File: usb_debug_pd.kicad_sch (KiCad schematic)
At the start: 83 parts, among them J7 Tag-Connect_TC2050-IDC-NL_2x5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, J8 USB-C_GCT_USB4105-GF-A, Q12 PJE138K, U29 W25Q80DV_USON, U30 TPS65988DHRSHR, U31 NTS0102_XSON, U32 NCP730BMT330_WSON, U34 FT230X_QFN, U39 TPS65988DHRSHR, U40 AP22615A_TSOT26, U42 TPD4E05U06QDQARQ1

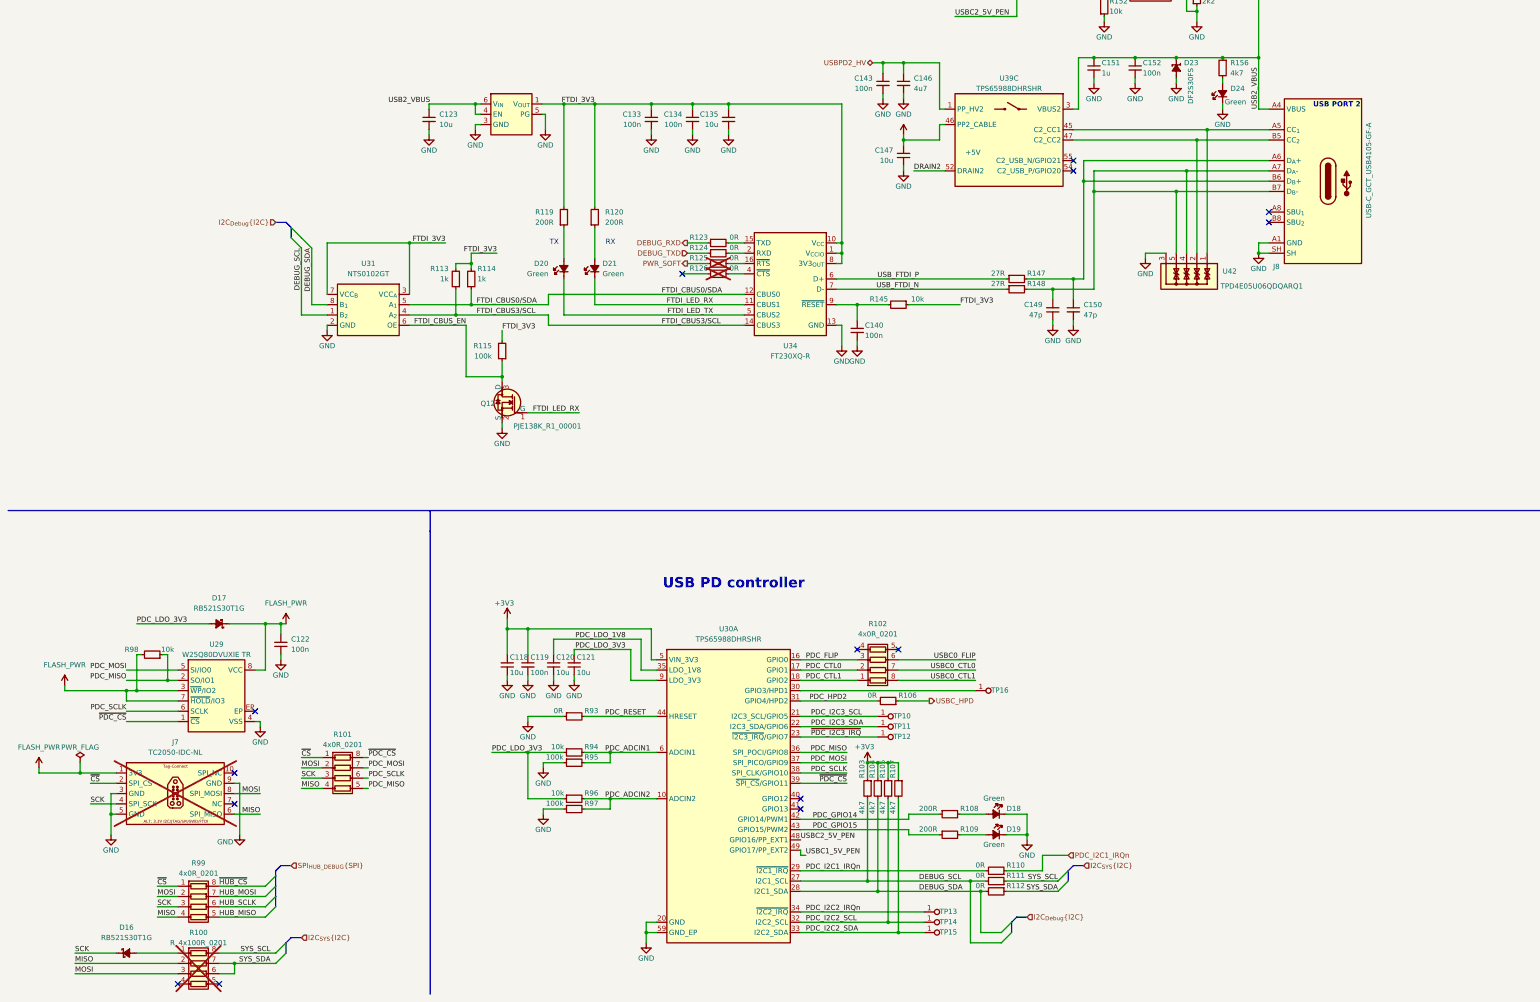
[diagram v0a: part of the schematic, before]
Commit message: [#82837] Start rerouting USB PD controller
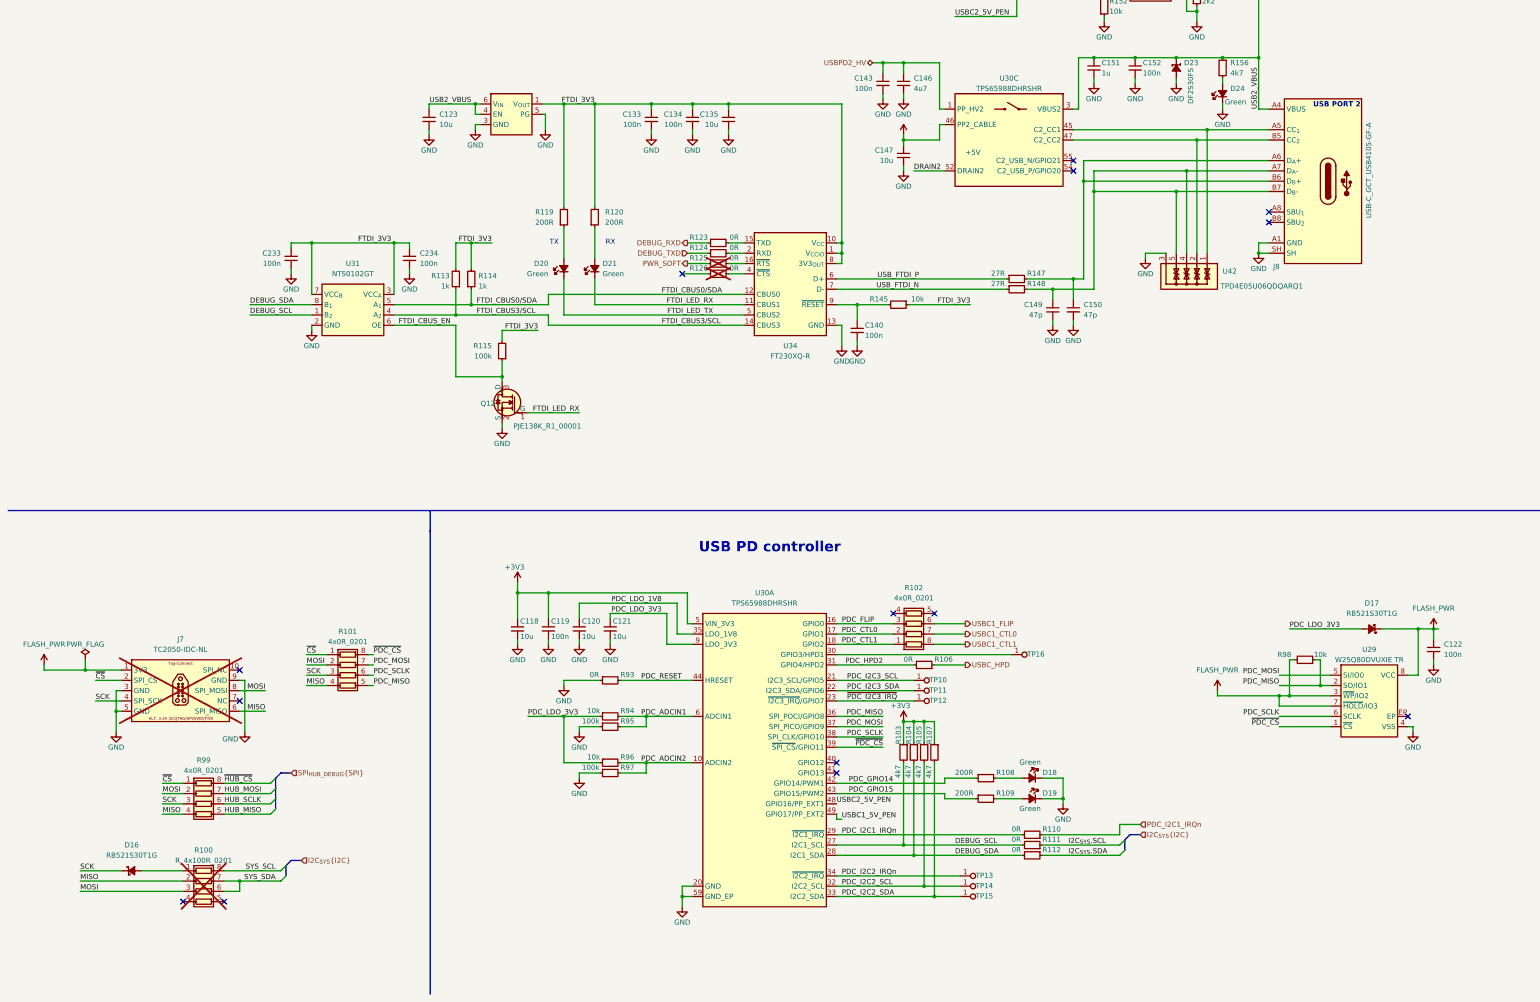
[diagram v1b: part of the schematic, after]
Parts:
- added C233, C234: C_100n_0402, antmicro-footprints:C_0402_1005Metric, symbol antmicroCapacitors0402:C_100n_0402
- renumbered U39 to U30
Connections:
- net FTDI_3V3: now also C233.1, C234.1
- net GND: now also C233.2, C234.2
- net SYS_SCL: no longer R111.1
- net SYS_SDA: no longer R112.1
- net USBC0_CTL0 renamed USBC1_CTL0
- net USBC0_CTL1 renamed USBC1_CTL1
- net USBC0_FLIP renamed USBC1_FLIP
- new net I2C_{SYS}.SCL: R111.1
- new net I2C_{SYS}.SDA: R112.1
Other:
- moved on the sheet: C118, C119, C120, C121, C122, D16, D17, D18, D19, J7, R100, R101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

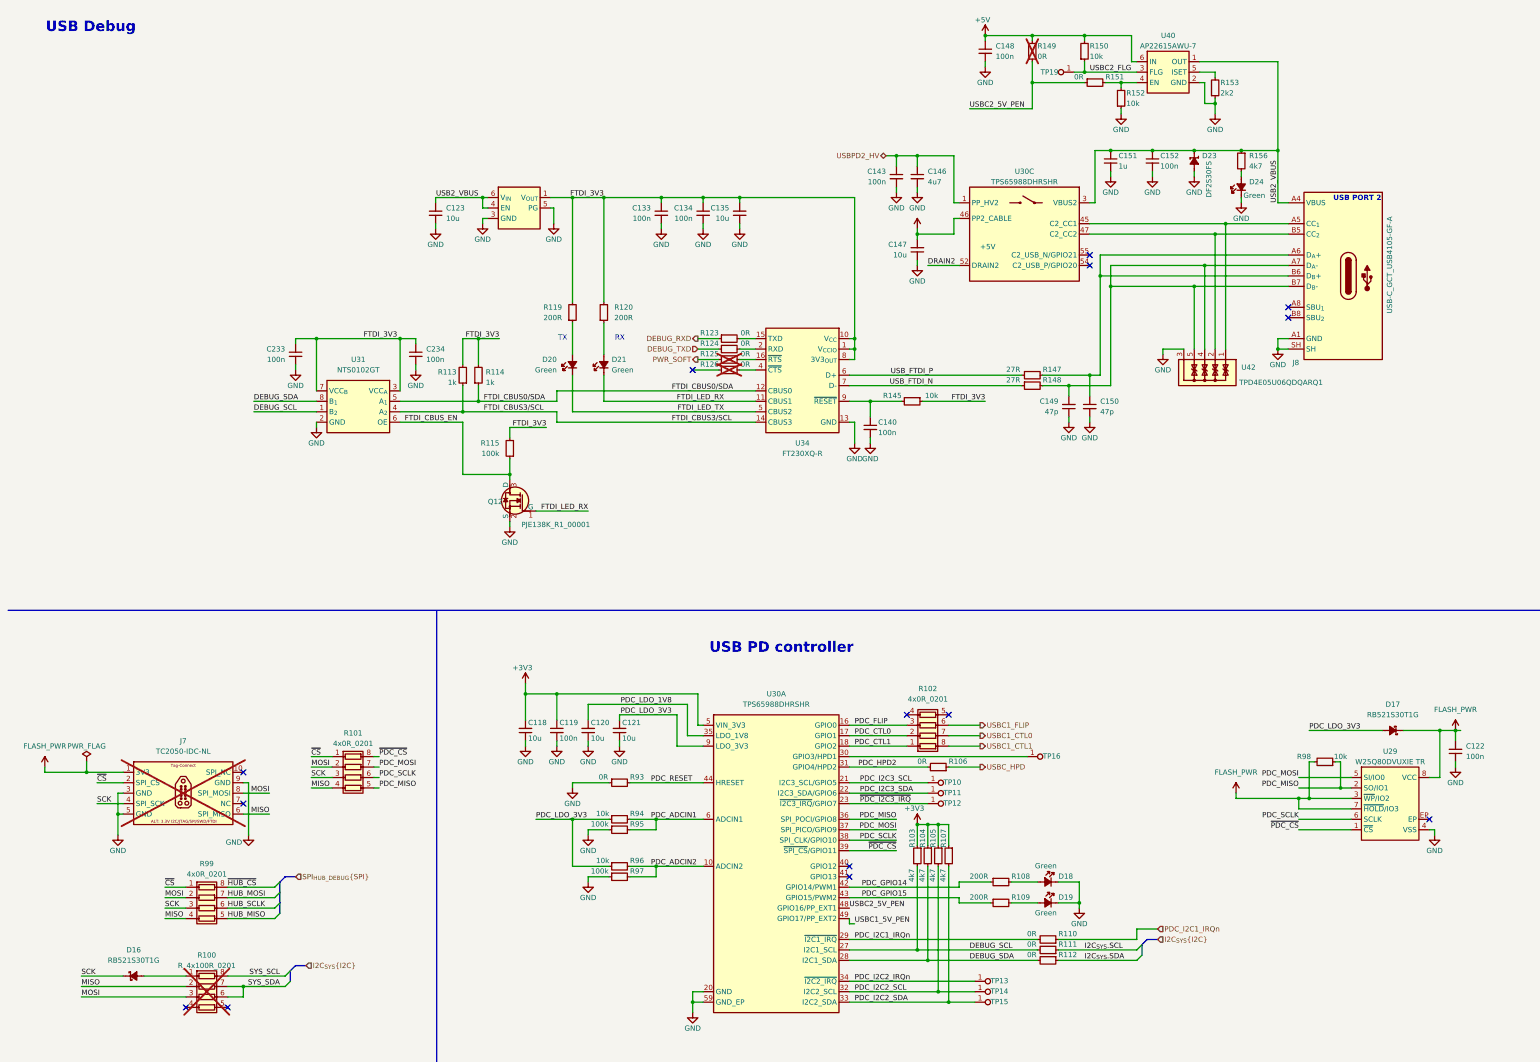
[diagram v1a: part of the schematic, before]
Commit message: [#82837] Finish rerouting USB PD controller, start debug section
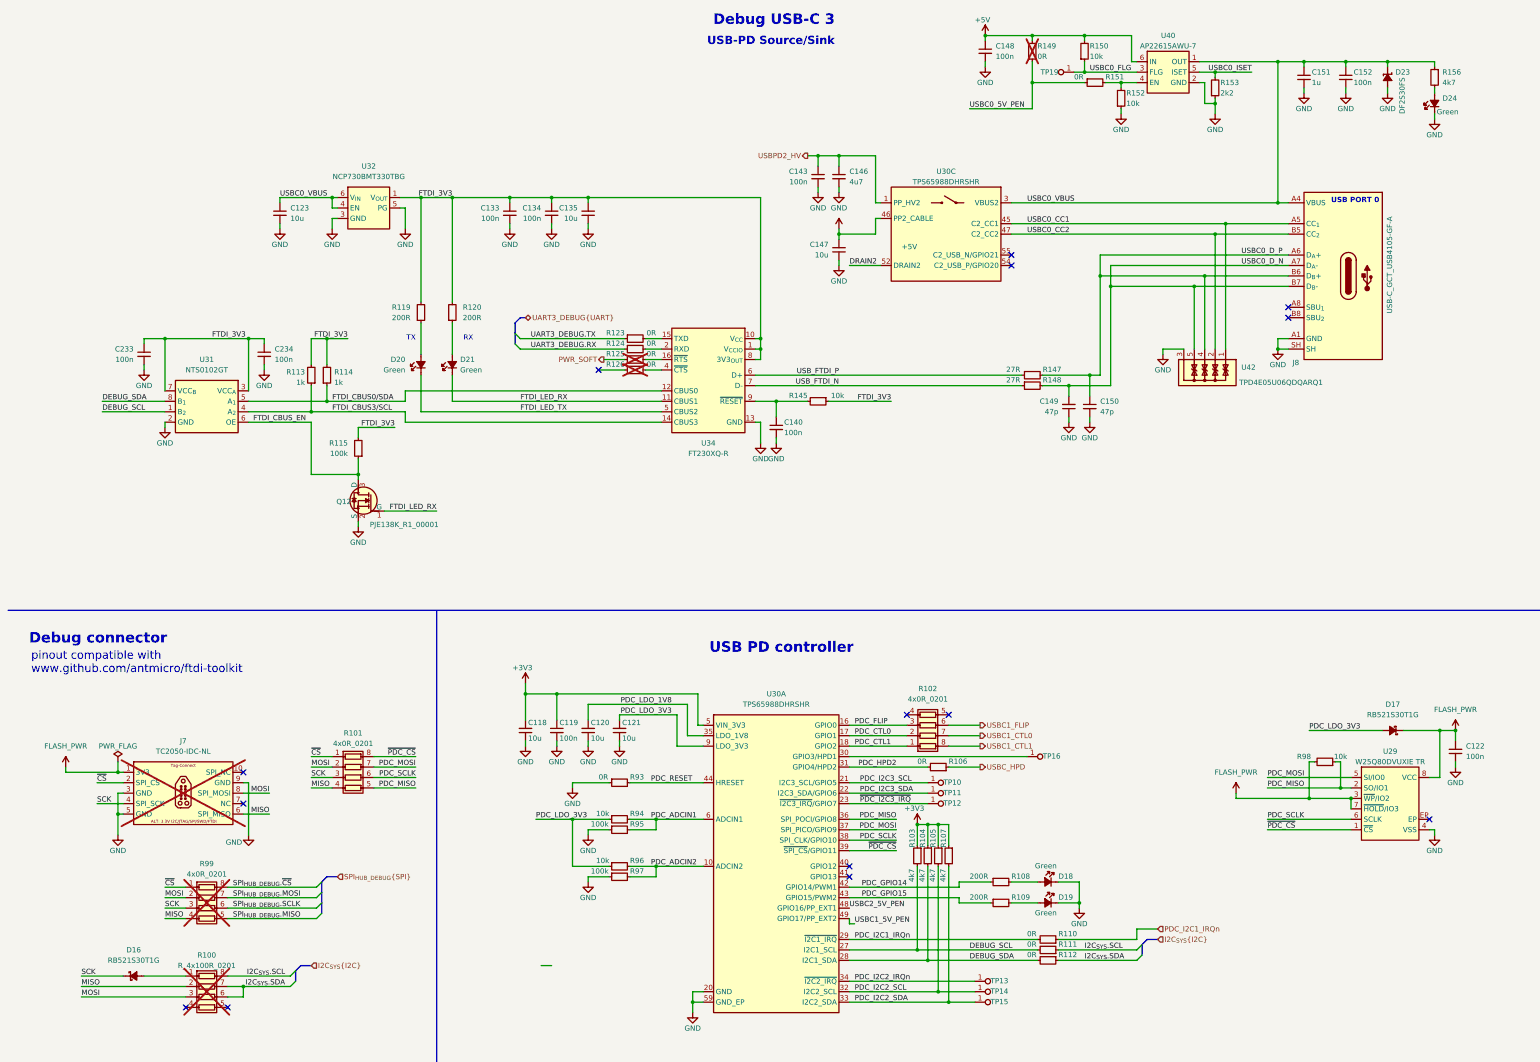
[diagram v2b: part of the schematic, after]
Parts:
- R99: now not fitted; now left out of the parts list
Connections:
- net SYS_SCL is gone; now on net I2C_{SYS}.SCL: R100.8 (R1.2)
- net SYS_SDA is gone; now on net I2C_{SYS}.SDA: R100.6 (R3.2), R100.7 (R2.2)
- net USBC2_5V_PEN: no longer R149.1, R151.1
- net USBC0_CC1: now reaches J8.A5 (CC_{1}), U30.45 (C2_CC1), U42.1, U42.10
- net USBC0_CC2: now reaches J8.B5 (CC_{2}), U30.47 (C2_CC2), U42.2, U42.9
- net USBC0_D_N: now reaches C149.2, J8.A7 (D_{A}-), J8.B7 (D_{B}-), R148.2, U42.5, U42.6
- net USBC0_D_N: no longer U42.4, U42.7
- net USBC0_D_P: now reaches C150.1, J8.A6 (D_{A}+), J8.B6 (D_{B}+), R147.2
- net USBC0_D_P: now also U42.4, U42.7
- net USBC0_ISET: now reaches R153.2, U40.5 (ISET)
- net DEBUG_RXD renamed UART3_DEBUG.TX
- net DEBUG_TXD renamed UART3_DEBUG.RX
- net HUB_MISO renamed SPI_{HUB_DEBUG}.MISO
- net HUB_MOSI renamed SPI_{HUB_DEBUG}.MOSI
- net HUB_SCLK renamed SPI_{HUB_DEBUG}.SCLK
- net USB2_VBUS renamed USBC0_VBUS
- net USBC2_FLG renamed USBC0_FLG
- net ~{HUB_CS} renamed SPI_{HUB_DEBUG}.~{CS}
- new net USBC0_5V_PEN: R149.1, R151.1
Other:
- note added: "Debug USB-C 3"
- note added: "Debug connector"
- note added: "USB PORT 0"
- note added: "USB-PD Source/Sink"
- note added: "pinout compatible with www.github.com/antmicro/ftdi-toolkit"
- note removed: "USB Debug"
- note removed: "USB PORT 2"
- moved on the sheet: C123, C133, C134, C135, C140, C143, C146, C147, C151, C152, C233, C234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
